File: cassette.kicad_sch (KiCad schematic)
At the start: 21 parts

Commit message: Fix wrong cap type in clock generator
Also fill some references automatically generated by KiCAD.
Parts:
- C22: renamed from C?; value (none) -> 100nF; footprint (none) -> artemisa:Disc_capacitor
- C32, C35: value (none) -> 1uF; footprint (none) -> artemisa:Radial_capacitor
- C33, C34: value (none) -> 22nF; footprint (none) -> artemisa:Disc_capacitor
- D3: value (none) -> 1N4448; footprint (none) -> artemisa:Axial_diode
- J8: value (none) -> DIN8; footprint (none) -> artemisa:DIN8
- K1: value (none) -> Relay; footprint (none) -> artemisa:Relay
- Q2: value (none) -> 2N2907; footprint (none) -> artemisa:TO92
- R13: renamed from R?; value (none) -> 2k2; footprint (none) -> artemisa:Axial_resistor
- R14, R15, R17: renamed from R?; value (none) -> 4k7; footprint (none) -> artemisa:Axial_resistor
- R16: renamed from R?; value (none) -> 100; footprint (none) -> artemisa:Axial_resistor
- R18: renamed from R?; value (none) -> 220k; footprint (none) -> artemisa:Axial_resistor
- R19: renamed from R?; value (none) -> 1k; footprint (none) -> artemisa:Axial_resistor
- R20: renamed from R?; value (none) -> 10k; footprint (none) -> artemisa:Axial_resistor
- R21, R22: renamed from R?; value (none) -> 2k7; footprint (none) -> artemisa:Axial_resistor
- U19: value (none) -> LM311; footprint (none) -> artemisa:DIP-8_300
- U19: renamed from U?; value (none) -> LM311; footprint (none) -> artemisa:DIP-8_300
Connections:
- net VCC: now reaches R19.2
- net VCC: now also C22.1, D3.2, K1.1, R18.2, R21.2, U19.8 (VCC)

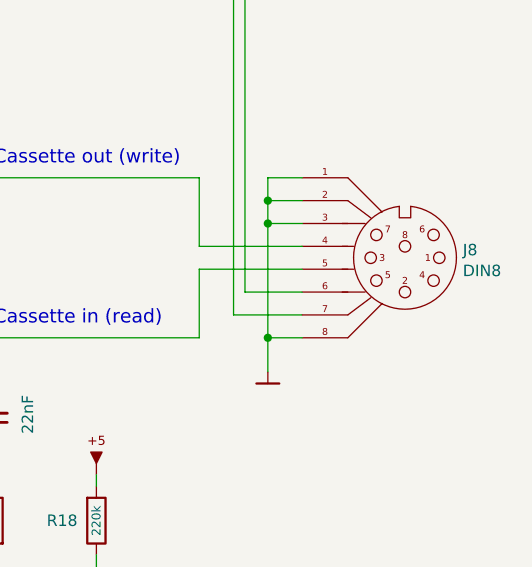
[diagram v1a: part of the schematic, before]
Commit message: Upgrade project files to KiCad v8
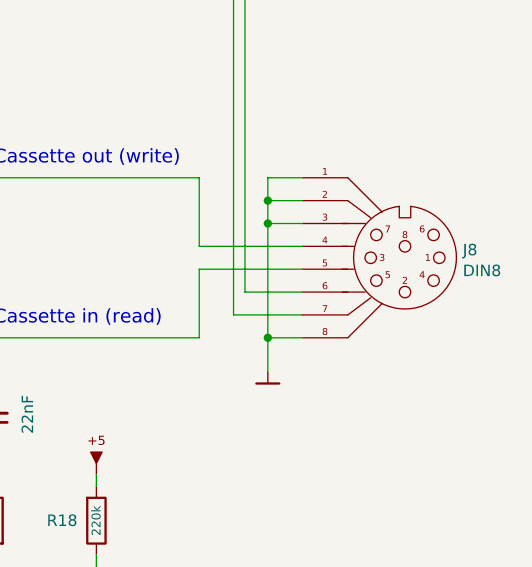
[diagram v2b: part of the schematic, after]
